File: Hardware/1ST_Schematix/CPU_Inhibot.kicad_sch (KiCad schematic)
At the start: 21 parts, among them J102 Conn_ST_STDC14, SW102 SW_Push, U1 STM32G431RBTx, Y1 Crystal_GND24_Small

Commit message: nom des compo
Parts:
- renumbered C114 to C201, C105 to C202, C104 to C203, C101 to C204, C102 to C205, C103 to C206, C106 to C207, D1 to D201, D2 to D202, J102 to J201, JP1 to JP201, JP2 to JP202, R1 to R201, R2 to R202, R3 to R203, R4 to R204, R15 to R205, R16 to R206, SW102 to SW201, U1 to U201, Y1 to Y201

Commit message: Bus I2C2
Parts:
- added R207, R208: 4.7k, Resistor_THT:R_Array_SIP4, symbol Device:R_Small
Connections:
- net +3.3V: now also R207.2, R208.2
- net SCL2: now reaches U201.22 (PC4)
- net SCL2: now also R207.1
- net SDA2: now reaches U201.42 (PA8)
- net SDA2: now also R208.1

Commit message: first
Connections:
- net SYS_SWCLK: now also U201.50 (PA14); no longer U201.36 (PB14)
- net SYS_SWDIO: now also U201.49 (PA13); no longer U201.35 (PB13)
- net TOF2_XST: now reaches U201.3 (PC14)
- net TOF1_GPIO: now reaches U201.37 (PB15)
- net TOF2_GPIO: now reaches U201.4 (PC15)
- net USART2_RX renamed Prog_Rx
- net USART2_TX renamed Prog_Tx
- new net TOF1_XST: U201.36 (PB14)

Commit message: Update before INT
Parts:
- R205, R206: now not fitted
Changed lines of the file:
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@@
 		(on_board yes)
 		(in_pos_files yes)
-		(dnp no)
+		(dnp yes)
 		(fields_autoplaced yes)
 		(property "Reference" "R205"
@@
 		(on_board yes)
 		(in_pos_files yes)
-		(dnp no)
+		(dnp yes)
 		(fields_autoplaced yes)
 		(property "Reference" "R206"

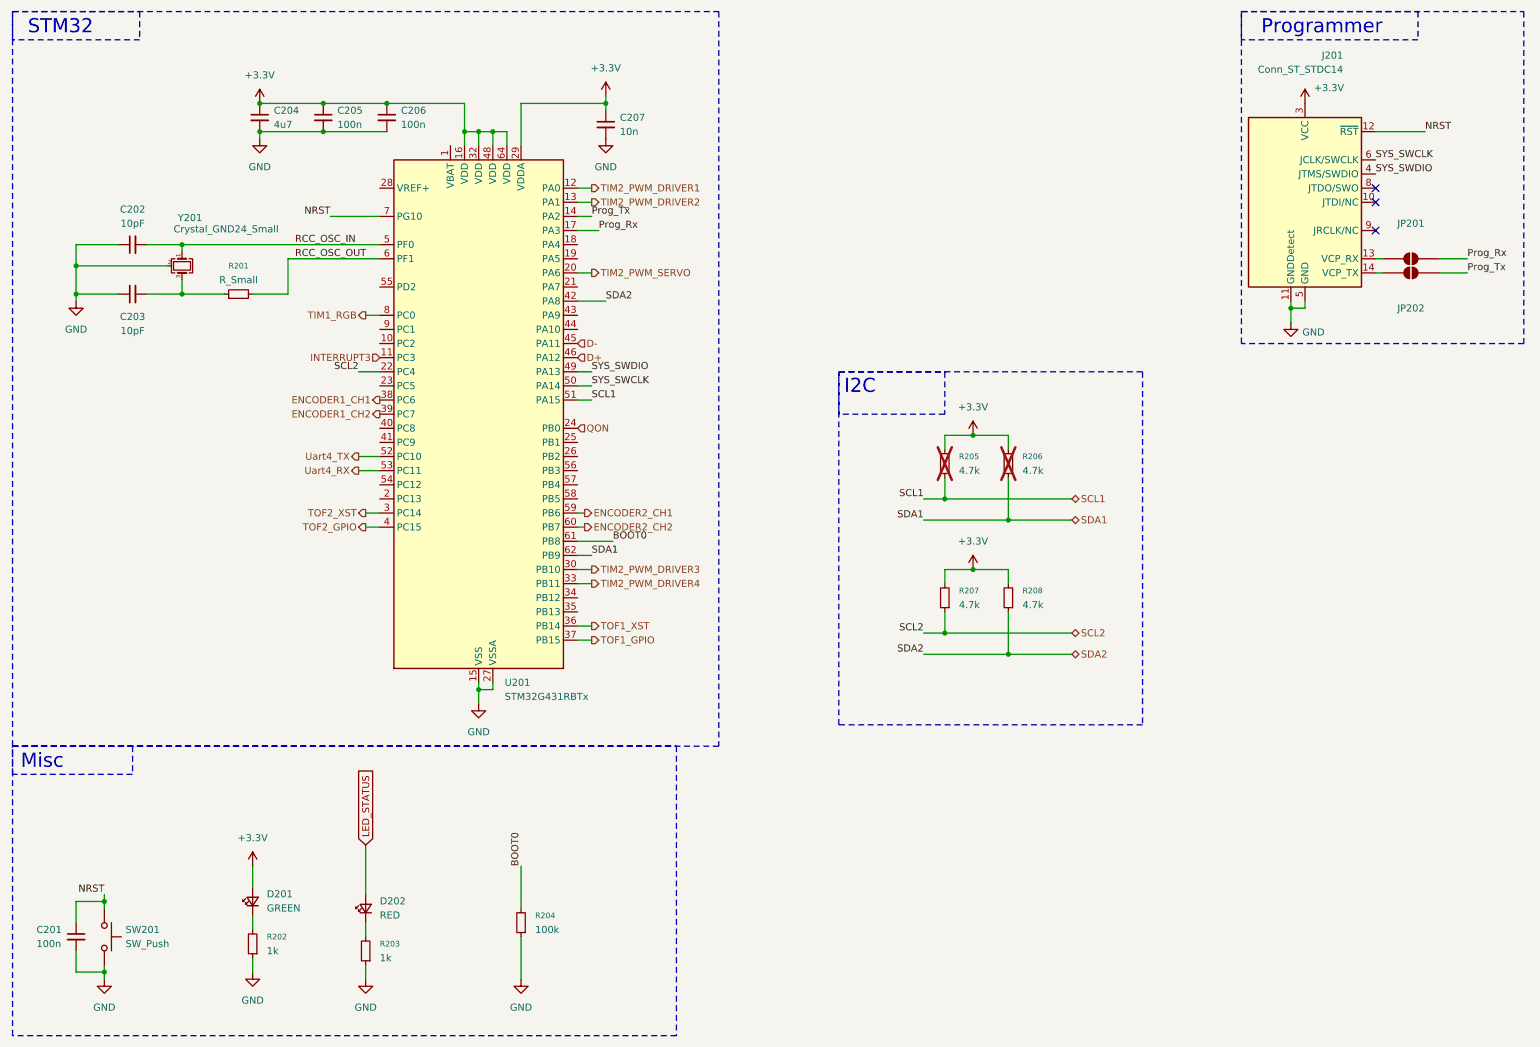
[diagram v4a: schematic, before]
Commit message: Update KiCad and STM32CubeMX
Ready for the check-in
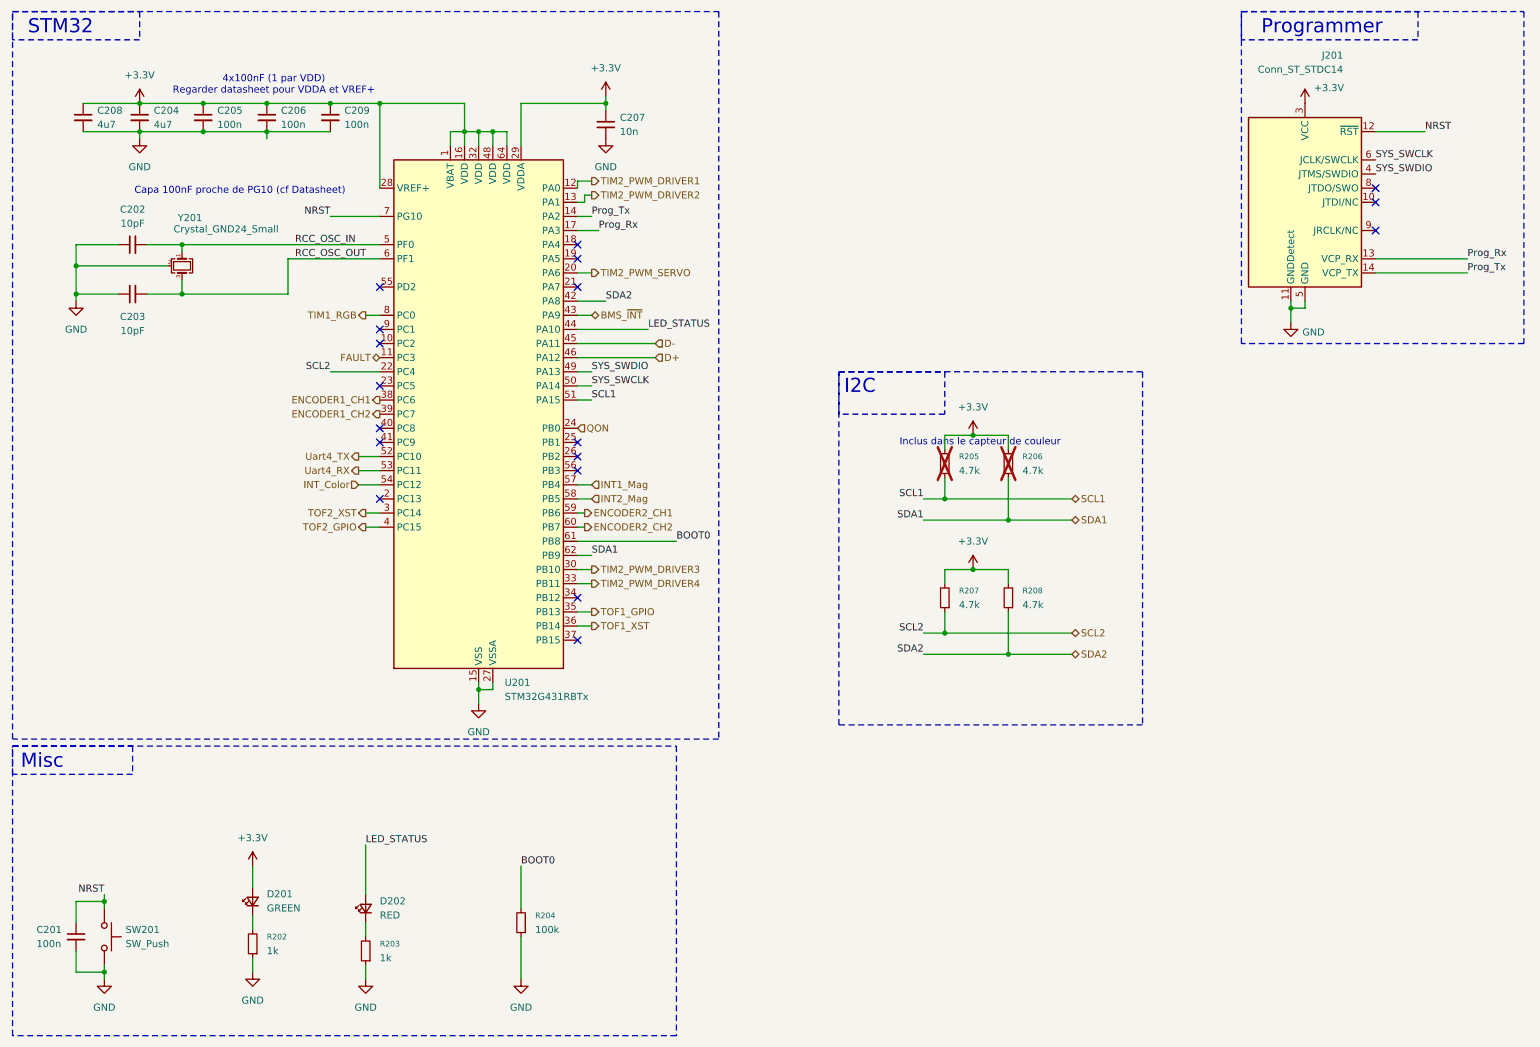
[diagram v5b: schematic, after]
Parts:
- removed JP201, JP202: SolderJumper_2_Open, Jumper:SolderJumper-2_P1.3mm_Open_TrianglePad1.0x1.5mm, symbol Jumper:SolderJumper_2_Open
- removed R201: R_Small, Resistor_THT:R_Array_SIP4, symbol Device:R_Small
- added C208: 4u7, Capacitor_SMD:C_0603_1608Metric, symbol Device:C_Small
- added C209: 100n, Capacitor_SMD:C_0402_1005Metric, symbol Device:C_Small
- SW201: footprint Button_Switch_SMD:SW_SPST_B3U-3000P -> Button_Switch_SMD:SW_Push_1P1T_NO_CK_KMR2
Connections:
- net +3.3V: now also U201.1 (VBAT), U201.28 (VREF+), C208.1, C209.1
- net GND: now also C208.2, C209.2
- net LED_STATUS: now also U201.44 (PA10)
- net Prog_Rx: now also J201.13 (VCP_RX)
- net Prog_Tx: now also J201.14 (VCP_TX)
- net RCC_OSC_OUT: now also C203.2, Y201.3
- net TOF1_GPIO: now also U201.35 (PB13); no longer U201.37 (PB15)
- net BMS_~{INT}: now reaches U201.43 (PA9)
- net INT_Color: now reaches U201.54 (PC12)
- net INT1_Mag: now reaches U201.57 (PB4)
- net INT2_Mag: now reaches U201.58 (PB5)
- net INTERRUPT3 renamed FAULT
- no-connect marks 3 -> 18
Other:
- note added: "4x100nF (1 par VDD) Regarder datasheet pour VDDA et VREF+"
- note added: "Capa 100nF proche de PG10 (cf Datasheet)"
- note added: "Inclus dans le capteur de couleur"
- moved on the sheet: C204, C205, C206

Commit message: schematic review with esteemed professor
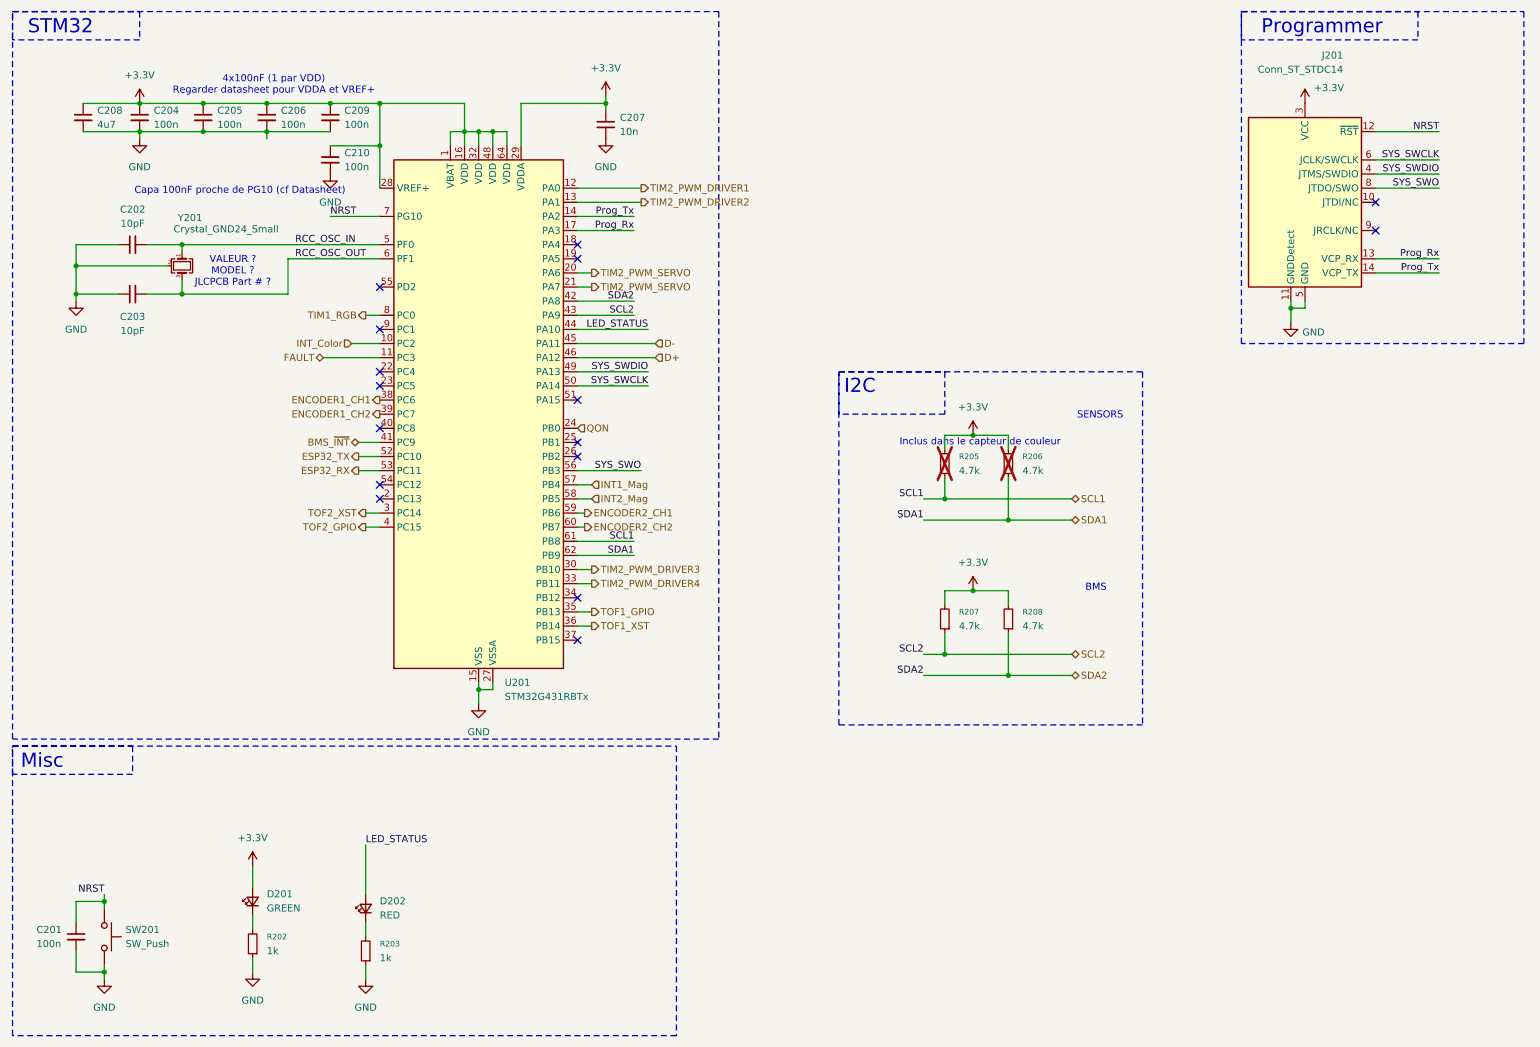
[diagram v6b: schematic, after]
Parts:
- removed R204: 100k, Resistor_THT:R_Array_SIP4, symbol Device:R_Small
- added C210: 100n, Capacitor_SMD:C_0402_1005Metric, symbol Device:C_Small
- C201, C205, C206, C209: JLCPCB Part # (none) -> C1525
- C202, C203, C208: footprint Capacitor_SMD:C_0603_1608Metric -> Capacitor_SMD:C_0402_1005Metric
- C204: value 4u7 -> 100n; footprint Capacitor_SMD:C_0603_1608Metric -> Capacitor_SMD:C_0402_1005Metric; JLCPCB Part # (none) -> C1525
- D201: footprint LED_SMD:LED_Cree-XHP50_3V_HighDensity -> LED_SMD:LED_0603_1608Metric
- D202: footprint (none) -> LED_SMD:LED_0603_1608Metric
- R202, R203, R207, R208: footprint Resistor_THT:R_Array_SIP4 -> Resistor_SMD:R_0402_1005Metric
- R205, R206: footprint Resistor_THT:R_Array_SIP4 -> Resistor_SMD:R_0603_1608Metric_Pad0.98x0.95mm_HandSolder
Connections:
- net BOOT0 is gone; now on net SCL1: U201.61 (PB8)
- net +3.3V: now also C210.1
- net BMS_~{INT}: now also U201.41 (PC9); no longer U201.43 (PA9)
- net GND: now also C210.2
- net INT_Color: now also U201.10 (PC2); no longer U201.54 (PC12)
- net SCL1: no longer U201.51 (PA15)
- net SCL2: now also U201.43 (PA9); no longer U201.22 (PC4)
- net TIM2_PWM_SERVO: now also U201.21 (PA7)
- net SYS_SWO: now reaches J201.8 (JTDO/SWO)
- net SYS_SWO: now also U201.56 (PB3)
- net Uart4_RX renamed ESP32_RX
- net Uart4_TX renamed ESP32_TX
- no-connect marks 18 -> 16
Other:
- note added: "BMS"
- note added: "SENSORS"
- note added: "VALEUR ? MODEL ? JLCPCB Part # ?"
- moved on the sheet: R207, R208

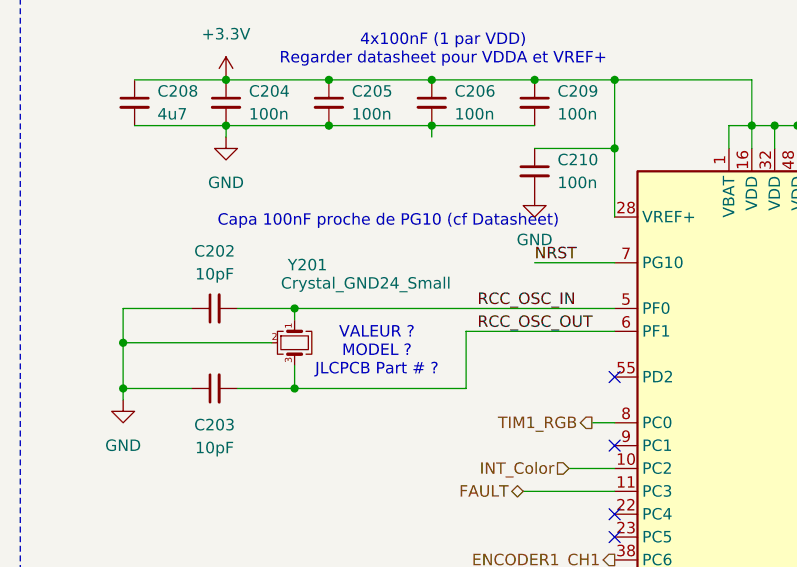
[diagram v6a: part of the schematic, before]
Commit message: prints for component except 10mOhm
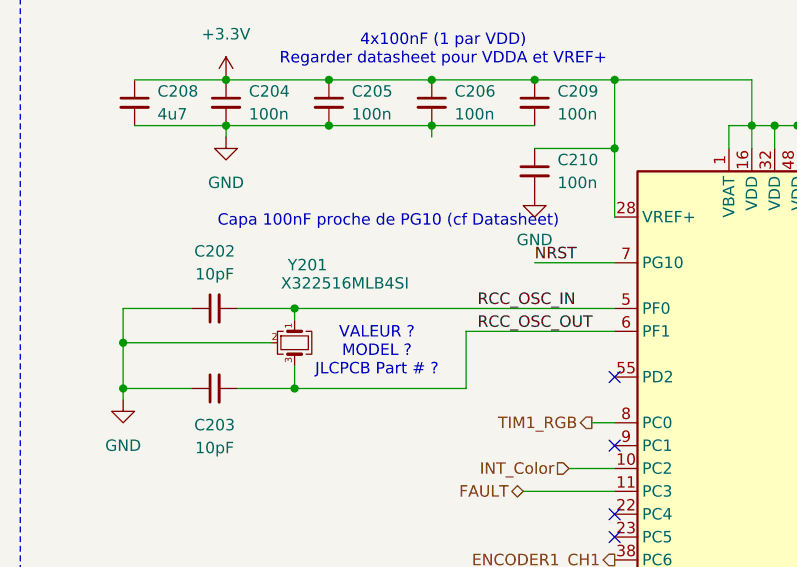
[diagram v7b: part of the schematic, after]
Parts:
- Y201: value Crystal_GND24_Small -> X322516MLB4SI; footprint Package_DFN_QFN:WDFN-10-1EP_3x3mm_P0.5mm_EP1.8x2.5mm -> Crystal:Crystal_SMD_EuroQuartz_MT-4Pin_3.2x2.5mm; JLCPCB Part # (none) -> C13738
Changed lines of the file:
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@@
 			)
 		)
-		(property "Value" "Crystal_GND24_Small"
+		(property "Value" "X322516MLB4SI"
 			(at 41.656 51.816 90)
 			(show_name no)
@@
 			)
 		)
-		(property "Footprint" "Package_DFN_QFN:WDFN-10-1EP_3x3mm_P0.5mm_EP1.8x2.5mm"
+		(property "Footprint" "Crystal:Crystal_SMD_EuroQuartz_MT-4Pin_3.2x2.5mm"
 			(at 43.18 58.42 0)
 			(hide yes)
@@
 			)
 		)
-		(property "Datasheet" ""
+		(property "Datasheet" "https://jlcpcb.com/partdetail/YXC_CrystalOscillators-X322516MLB4SI/C13738"
 			(at 43.18 58.42 0)
 			(hide yes)
@@
 			(do_not_autoplace no)
 			(effects
+				(font
+					(size 1.27 1.27)
+				)
+			)
+		)
+		(property "JLCPCB Part #" "C13738"
+			(at 43.18 58.42 90)
+			(hide yes)
+			(show_name no)
+			(do_not_autoplace no)
+			(effects
